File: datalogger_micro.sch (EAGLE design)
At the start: 46 parts, among them IC1 DS3231/SO, IC2 LD117AS33TR, M1 PAT, M2 PAT, Q2 IRLML5203

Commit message: MOSFET fix
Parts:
- added R19: 100k, SparkFun:RESISTOR0603-RES
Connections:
- removed net N$1: IC2.ADJ, Q2.S
- new net N$10: C6.1, IC2.IN, Q2.D
- new net N$11: Q2.G, R12.1, R19.2
- net GND: now also IC2.ADJ; no longer Q2.D, R12.2
- net N$5: now also M2.1; no longer M1.1
- net N$6: now also M1.1; no longer M2.1
- net N$8: now also M2.2; no longer M1.2
- net N$9: now also M1.2; no longer M2.2
- net VBAT: now also Q2.S, R19.1; no longer C6.1, IC2.IN
- net VCC/ST_ON: now also R12.2; no longer Q2.G, R12.1
- net VDIV1: now also VD1.2; no longer VD2.2
- net VDIV2: now also VD2.2; no longer VD1.2
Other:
- moved on the sheet: C6, M1, M2, Q2, R12, VD1, VD2

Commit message: SST25 Layout
pins 5-8 were switched
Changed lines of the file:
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@@
 <?xml version="1.0" encoding="utf-8"?>
 <!DOCTYPE eagle SYSTEM "eagle.dtd">
-<eagle version="7.2.0">
+<eagle version="7.3.0">
 <drawing>
 <settings>

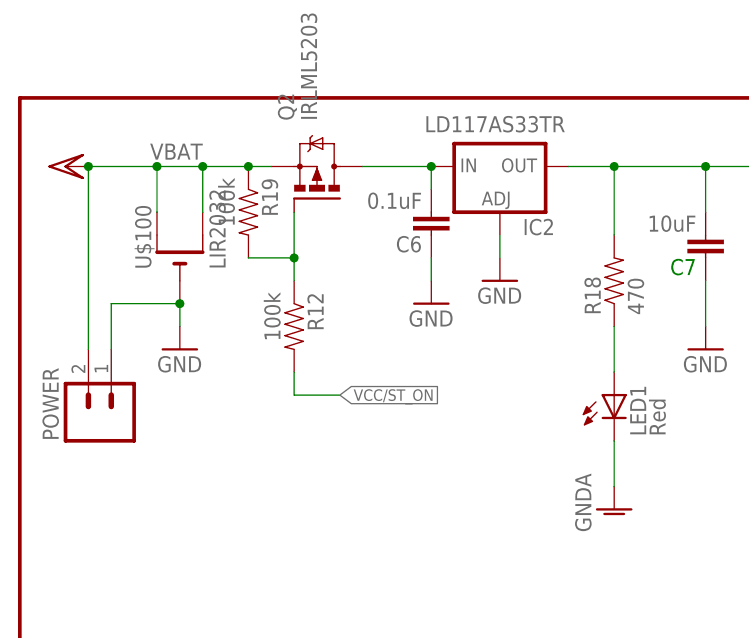
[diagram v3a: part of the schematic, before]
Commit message: VCC-ST active low
VCC ST is now active low by p channel mosfet
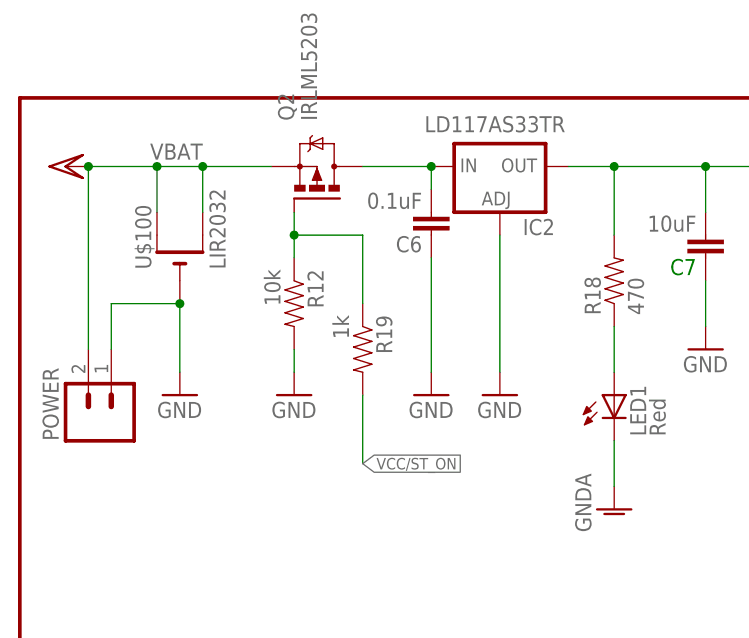
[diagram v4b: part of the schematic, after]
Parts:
- R12: value 100k -> 10k
- R19: value 100k -> 1k
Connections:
- net GND: now also R12.2
- net N$11: now also R19.1; no longer R19.2
- net VBAT: no longer R19.1
- net VCC/ST_ON: now also R19.2; no longer R12.2
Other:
- moved on the sheet: R12, R19
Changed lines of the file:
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@@
 <part name="VCC-BAT1" library="supply1" deviceset="VCC/2" device=""/>
 <part name="VCC-BAT2" library="supply1" deviceset="VCC/2" device=""/>
-<part name="R12" library="SparkFun" deviceset="RESISTOR" device="0603-RES" value="100k"/>
+<part name="R12" library="SparkFun" deviceset="RESISTOR" device="0603-RES" value="10k"/>
 <part name="GND15" library="SparkFun" deviceset="GND" device=""/>
 <part name="32.768KHZ" library="crystal" deviceset="CRYSTAL" device="TC38H"/>
@@
 <part name="SPI" library="SparkFun-Connectors" deviceset="AVR_SPI_PRG_6" device="PTH"/>
 <part name="Q2" library="transistor-power" deviceset="IRLML5203" device=""/>
-<part name="R19" library="SparkFun" deviceset="RESISTOR" device="0603-RES" value="100k"/>
+<part name="R19" library="SparkFun" deviceset="RESISTOR" device="0603-RES" value="1k"/>
+<part name="GND1" library="SparkFun" deviceset="GND" device=""/>
 </parts>
 <sheets>
@@
 <attribute name="VALUE" x="235.966" y="95.123" size="1.778" layer="96" rot="R180"/>
 </instance>
-<instance part="GND32" gate="1" x="45.72" y="162.56"/>
+<instance part="GND32" gate="1" x="45.72" y="152.4"/>
 <instance part="GND4" gate="1" x="142.24" y="121.92"/>
 <instance part="JP1" gate="G$1" x="27.94" y="106.68"/>
@@
 <instance part="VCC-BAT1" gate="G$1" x="175.26" y="68.58" smashed="yes"/>
 <instance part="VCC-BAT2" gate="G$1" x="121.92" y="48.26" smashed="yes" rot="R90"/>
-<instance part="R12" gate="G$1" x="30.48" y="160.02" rot="R270"/>
-<instance part="GND15" gate="1" x="53.34" y="165.1"/>
+<instance part="R12" gate="G$1" x="30.48" y="162.56" rot="R270"/>
+<instance part="GND15" gate="1" x="53.34" y="152.4"/>
 <instance part="32.768KHZ" gate="G$1" x="144.78" y="134.62" smashed="yes" rot="R270">
 <attribute name="NAME" x="140.462" y="140.97" size="1.778" layer="95" rot="R270"/>
@@
 <instance part="R15" gate="G$1" x="86.36" y="68.58"/>
 <instance part="GND17" gate="1" x="81.28" y="60.96" rot="MR0"/>
-<instance part="GND18" gate="1" x="17.78" y="157.48"/>
+<instance part="GND18" gate="1" x="17.78" y="152.4"/>
 <instance part="C1" gate="G$1" x="175.26" y="58.42" smashed="yes" rot="R180">
 <attribute name="NAME" x="176.276" y="58.547" size="1.778" layer="95"/>
@@
 <instance part="SPI" gate="G$1" x="66.04" y="104.14"/>
 <instance part="Q2" gate="G$1" x="33.02" y="175.26" rot="R90"/>
-<instance part="R19" gate="G$1" x="25.4" y="172.72" rot="R270"/>
+<instance part="R19" gate="G$1" x="38.1" y="157.48" rot="R270"/>
+<instance part="GND1" gate="1" x="30.48" y="152.4"/>
 </instances>
 <busses>
@@
 <pinref part="GND32" gate="1" pin="GND"/>
 <pinref part="C6" gate="G$1" pin="2"/>
-<wire x1="45.72" y1="165.1" x2="45.72" y2="167.64" width="0.1524" layer="91"/>
+<wire x1="45.72" y1="154.94" x2="45.72" y2="167.64" width="0.1524" layer="91"/>
 </segment>
 <segment>
@@
 <segment>
 <pinref part="GND15" gate="1" pin="GND"/>
-<wire x1="53.34" y1="170.18" x2="53.34" y2="167.64" width="0.1524" layer="91"/>
+<wire x1="53.34" y1="170.18" x2="53.34" y2="154.94" width="0.1524" layer="91"/>
 <pinref part="IC2" gate="G$1" pin="ADJ"/>
 </segment>
@@
 <wire x1="10.16" y1="157.48" x2="10.16" y2="162.56" width="0.1524" layer="91"/>
 <wire x1="10.16" y1="162.56" x2="17.78" y2="162.56" width="0.1524" layer="91"/>
-<wire x1="17.78" y1="162.56" x2="17.78" y2="160.02" width="0.1524" layer="91"/>
+<wire x1="17.78" y1="162.56" x2="17.78" y2="154.94" width="0.1524" layer="91"/>
 <junction x="17.78" y="162.56"/>
 </segment>
@@
 <label x="81.28" y="101.6" size="1.778" layer="95"/>
 <pinref part="SPI" gate="G$1" pin="6"/>
+</segment>
+<segment>
+<pinref part="GND1" gate="1" pin="GND"/>
+<pinref part="R12" gate="G$1" pin="2"/>
+<wire x1="30.48" y1="154.94" x2="30.48" y2="157.48" width="0.1524" layer="91"/>
 </segment>
 </net>
@@
 </segment>
 <segment>
-<label x="35.56" y="152.4" size="1.27" layer="95" xref="yes"/>
-<pinref part="R12" gate="G$1" pin="2"/>
-<wire x1="35.56" y1="152.4" x2="30.48" y2="152.4" width="0.1524" layer="91"/>
-<wire x1="30.48" y1="152.4" x2="30.48" y2="154.94" width="0.1524" layer="91"/>
+<label x="38.1" y="144.78" size="1.27" layer="95" xref="yes"/>
+<wire x1="38.1" y1="144.78" x2="38.1" y2="152.4" width="0.1524" layer="91"/>
+<pinref part="R19" gate="G$1" pin="2"/>
 </segment>
 </net>
@@
 <junction x="7.62" y="177.8"/>
 <pinref part="Q2" gate="G$1" pin="S"/>
-<wire x1="20.32" y1="177.8" x2="25.4" y2="177.8" width="0.1524" layer="91"/>
+<wire x1="20.32" y1="177.8" x2="27.94" y2="177.8" width="0.1524" layer="91"/>
 <junction x="20.32" y="177.8"/>
-<pinref part="R19" gate="G$1" pin="1"/>
-<junction x="25.4" y="177.8"/>
-<wire x1="25.4" y1="177.8" x2="27.94" y2="177.8" width="0.1524" layer="91"/>
 </segment>
 <segment>
@@
 <net name="N$11" class="0">
 <segment>
-<pinref part="R19" gate="G$1" pin="2"/>
-<wire x1="25.4" y1="167.64" x2="30.48" y2="167.64" width="0.1524" layer="91"/>
 <pinref part="R12" gate="G$1" pin="1"/>
-<wire x1="30.48" y1="165.1" x2="30.48" y2="167.64" width="0.1524" layer="91"/>
 <pinref part="Q2" gate="G$1" pin="G"/>
-<wire x1="30.48" y1="167.64" x2="30.48" y2="172.72" width="0.1524" layer="91"/>
-<junction x="30.48" y="167.64"/>
-</segment>
-</net>
+<wire x1="30.48" y1="167.64" x2="30.48" y2="170.18" width="0.1524" layer="91"/>
+<pinref part="R19" gate="G$1" pin="1"/>
+<wire x1="30.48" y1="170.18" x2="30.48" y2="172.72" width="0.1524" layer="91"/>
+<wire x1="38.1" y1="162.56" x2="38.1" y2="170.18" width="0.1524" layer="91"/>
+<wire x1="38.1" y1="170.18" x2="30.48" y2="170.18" width="0.1524" layer="91"/>
+<junction x="30.48" y="170.18"/>
+</segment>
+</net>
